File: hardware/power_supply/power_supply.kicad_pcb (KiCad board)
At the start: 2 copper layers, 45.5 x 30 mm, 14 parts, among them J1 Conn_01x04, J2 Conn_01x02, J3 Conn_01x02, U1 LM2596

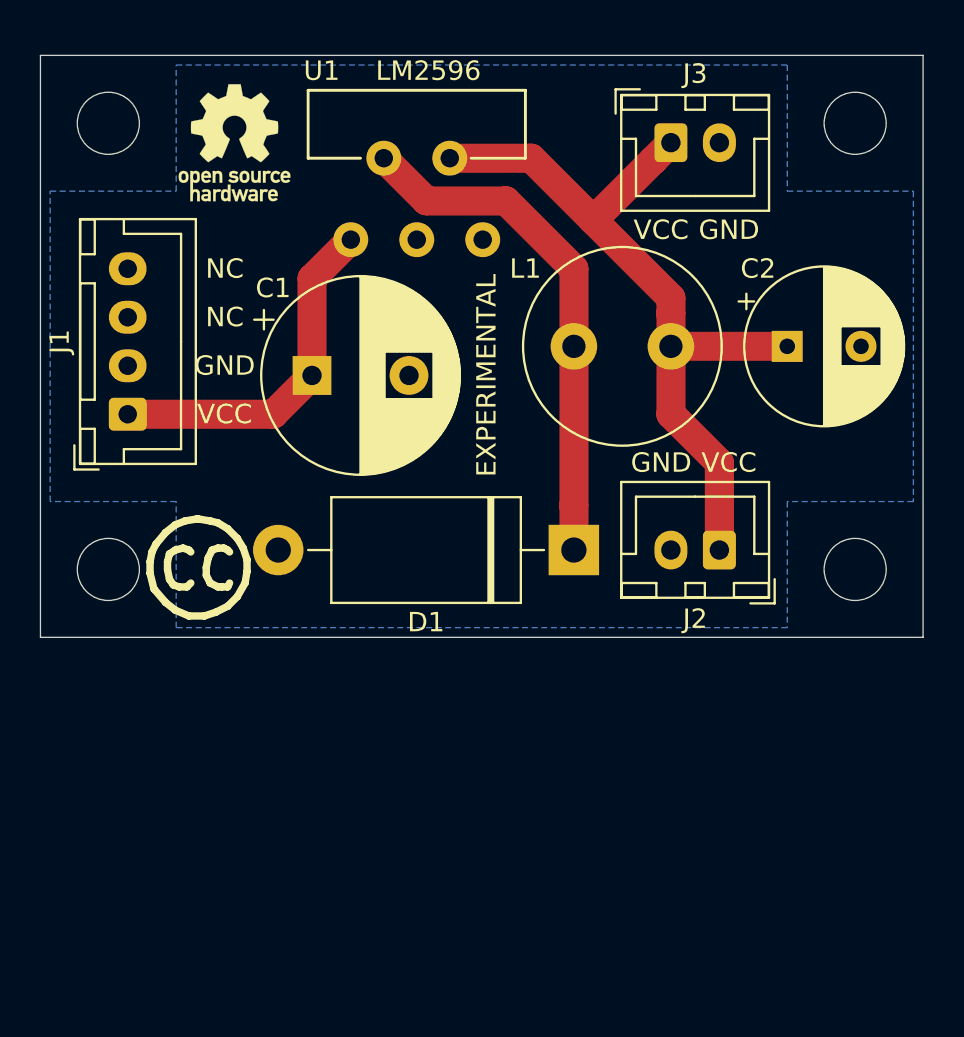
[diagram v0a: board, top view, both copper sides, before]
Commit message: update power supply
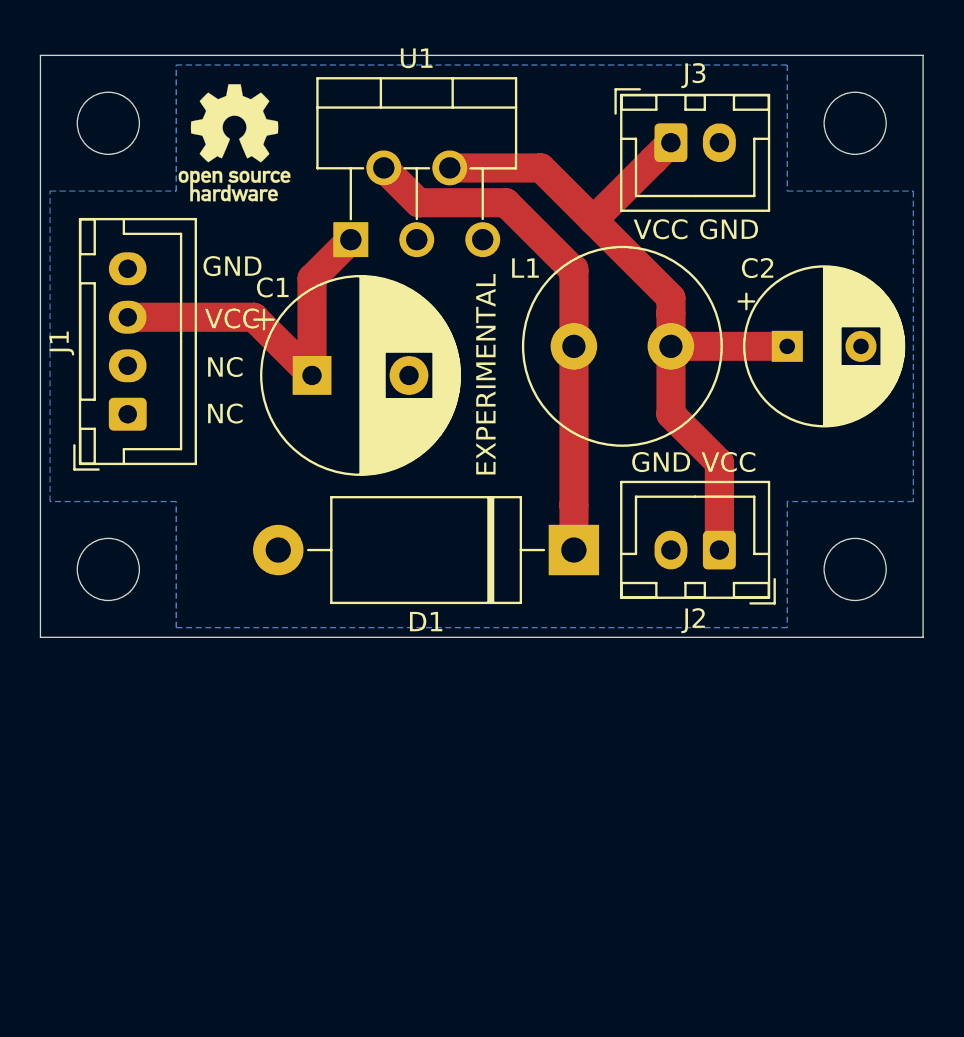
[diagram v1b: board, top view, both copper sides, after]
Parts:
- removed the REF** at (166.5, 138.5)
- U1: value LM2596 -> LM2596S-5; footprint Flypi:LM2596 -> Package_TO_SOT_THT:TO-220-5_P3.4x3.7mm_StaggerOdd_Lead3.8mm_Vertical
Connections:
- J1 pad 1: Net-(C1-Pad1) -> Net-(J1-Pad1)
- J1 pad 2: GND -> Net-(J1-Pad2)
- J1 pad 3: Net-(J1-Pad3) -> Net-(C1-Pad1)
- J1 pad 4: Net-(J1-Pad4) -> GND
- J3 pad 2: Net-(C2-Pad1) -> GND

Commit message: Update on 12V5A system power line
- 12V5A power line is now represented by two connectors with 2 pins across all the modules
- all .png previews are updated. The central hub now has previews for schematics, PCB tracing and 3D model
- peltier module now has two 12V5A connectors with redesigned one side of the bridge. Now all MOSFETs can be equipped with heatsinks
- hum/temp sensor now has its connector position reversed to mimic Grove's one
- hum/temp and gas sensors now have a small BeeHive logo on front layer rather than one big on back layer
- hum/temp sensor now use only one layer for signals and one layer for ground
- switch arrays now have two connectors for 12V5A and 5V3A power lines
- switch arrays had their power lines better traced (no sharp turns)
- power supply (12V5A to 5V3A) now has two connectors for 12V5A power line
- one trace of power supply, which lies in between LM2596's legs, was narrowed to ensure that it will not be accidentally soldered or damaged during placement
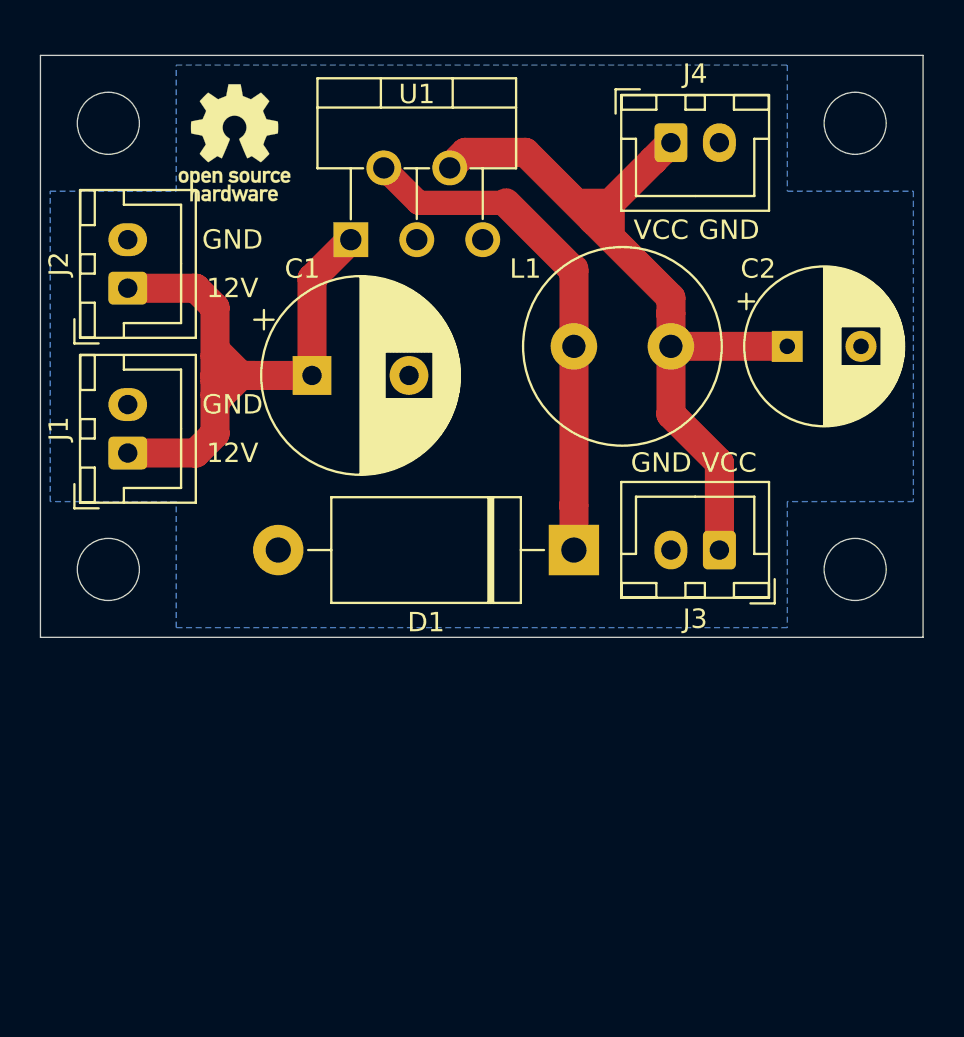
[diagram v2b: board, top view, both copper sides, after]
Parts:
- added J2: Conn_01x02, Connector_JST:JST_XH_B2B-XH-A_1x02_P2.50mm_Vertical, F.Cu at (163.0, 124.0)
- J1: value Conn_01x04 -> Conn_01x02; footprint Connector_JST:JST_XH_B4B-XH-A_1x04_P2.50mm_Vertical -> Connector_JST:JST_XH_B2B-XH-A_1x02_P2.50mm_Vertical
- moved J1 2.00 mm to (163.0, 132.5)
- renumbered J2 to J3, J3 to J4
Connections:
- J1 pad 1: Net-(J1-Pad1) -> Net-(C1-Pad1)
- J1 pad 2: Net-(J1-Pad2) -> GND
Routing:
- net Net-(C1-Pad1): track 18.6 -> 33.9 mm
- net Net-(C2-Pad1): track 39.9 -> 44.5 mm
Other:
- rule pad_to_mask_clearance: 0.051 -> 0
- board text added: "12V"
- board text removed: "EXPERIMENTAL"
- board text removed: "NC"

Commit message: Update 5V3A breakout
- added LED for 12V5A line;
- added two 5V3A line connectors added;
- implemented board version as text marking on PCB;
- changed the size of PCB to match others;
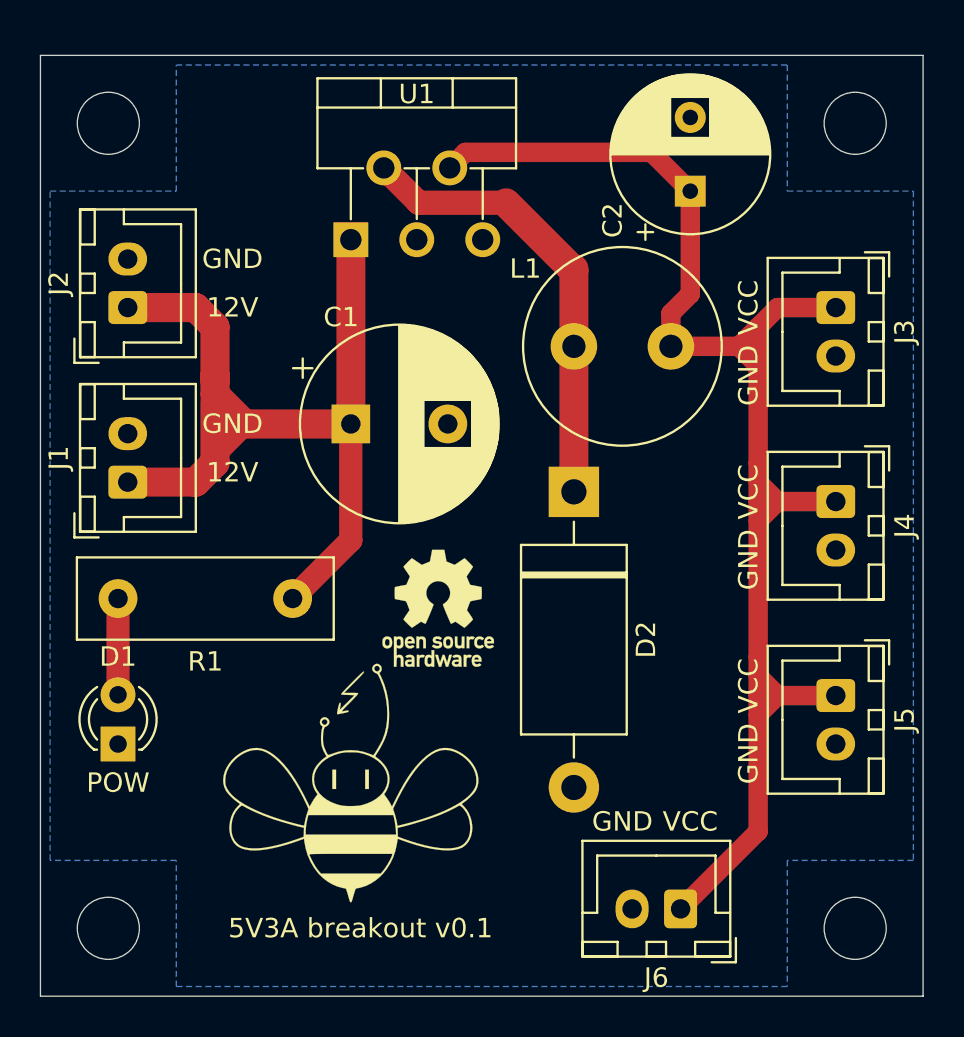
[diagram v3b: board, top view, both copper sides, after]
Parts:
- added D1: LED, LED_THT:LED_D3.0mm, F.Cu at (162.5, 147.5)
- added G***: LOGO, logo-beehive:logo-beehive-13_2х12_3mm, F.Cu at (174.5, 149.5)
- added J5: Conn_01x02, Connector_JST:JST_XH_B2B-XH-A_1x02_P2.50mm_Vertical, F.Cu at (199.5, 145.0)
- added J6: Conn_01x02, Connector_JST:JST_XH_B2B-XH-A_1x02_P2.50mm_Vertical, F.Cu at (191.5, 156.0)
- added R1: 560, Resistor_THT:R_Box_L13.0mm_W4.0mm_P9.00mm, F.Cu at (171.5, 140.0)
- moved REF** 26.2 mm to (179.0, 140.5)
- moved J4 20.4 mm to (199.5, 135.0), turned to 270 degrees
- moved REF** 18.5 mm to (200.5, 157.0)
- moved REF** 18.5 mm to (162.0, 157.0)
- moved J3 13.9 mm to (199.5, 125.0), turned to 270 degrees
- moved C2 9.43 mm to (192.0, 119.0), turned to 90 degrees
- moved C1 3.20 mm to (174.5, 131.0)
- moved D2 3.00 mm to (186.0, 134.5), turned to 270 degrees
- moved J1 1.50 mm to (163.0, 134.0)
- moved J2 1.00 mm to (163.0, 125.0)
- renumbered D1 to D2
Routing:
- net Net-(C2-Pad1): track 44.5 -> 78.5 mm
- net Net-(C1-Pad1): track 33.9 -> 46.3 mm
- net Net-(D1-Pad2): track 0.00 -> 4.96 mm
- net Net-(D2-Pad1): track 26.5 -> 23.0 mm
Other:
- board size 45.5 x 30 mm -> 45.5 x 48.5 mm
- board text added: "5V3A breakout v0.1"
- board text added: "POW"

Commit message: Apply CERN-W license
Apply CERN-W license to all boards, move the first iteration of the IR_sensor to the archive

Co-Authored-By: Andre Maia Chagas <a.maia-chagas@sussex.ac.uk>
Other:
- board text added: "board by Ihor Sobianin licensed under CERN-OHL-W 2.0 https://ohwr.org/project/cernohl"

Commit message: Add USB footprint to 5V power supply
Add USB footprint to the 12V to 5V converter. It is a continuation of the idea to free space on the main hub because of USB irrelevancy there
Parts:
- added J7: USB_A, Connector_USB:USB_A_Wuerth_614004134726_Horizontal, F.Cu at (178.5, 146.0)
- moved REF** 26.0 mm to (169.0, 116.5)
- moved G*** 4.27 mm to (170.5, 151.0)
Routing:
- net Net-(C2-Pad1): track 78.5 -> 100.8 mm
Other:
- net class Default removed
- board text added: "5V3A breakout v0.2"
- board text removed: "5V3A breakout v0.1"
